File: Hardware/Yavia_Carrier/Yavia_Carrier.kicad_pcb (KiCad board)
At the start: 2 copper layers, 93.5 x 40 mm, 107 parts, among them J1 Power, J10 52610-1572, J11 USB, J12 Ethernet, J2 Serial, J3 STRB_IS, J4 STRB_IS, J5 STRB, J6 STRB, J7 52610-1572, J8 FLASH, J9 FLASH, Q1 MMBT2222ALT1G, Q2 MMBT2222ALT1G, T1 HX1188NL, U1 Verdin iMX8M Plus, U10 LAN9512i, U2 AP63203, U3 LM3671, U4 TCMT1103, U5 TCMT1103, U6 LDD600L, U7 LDD600L, U8 74AHC1G32, U9 74AHC1G32, Y1 25MHZ

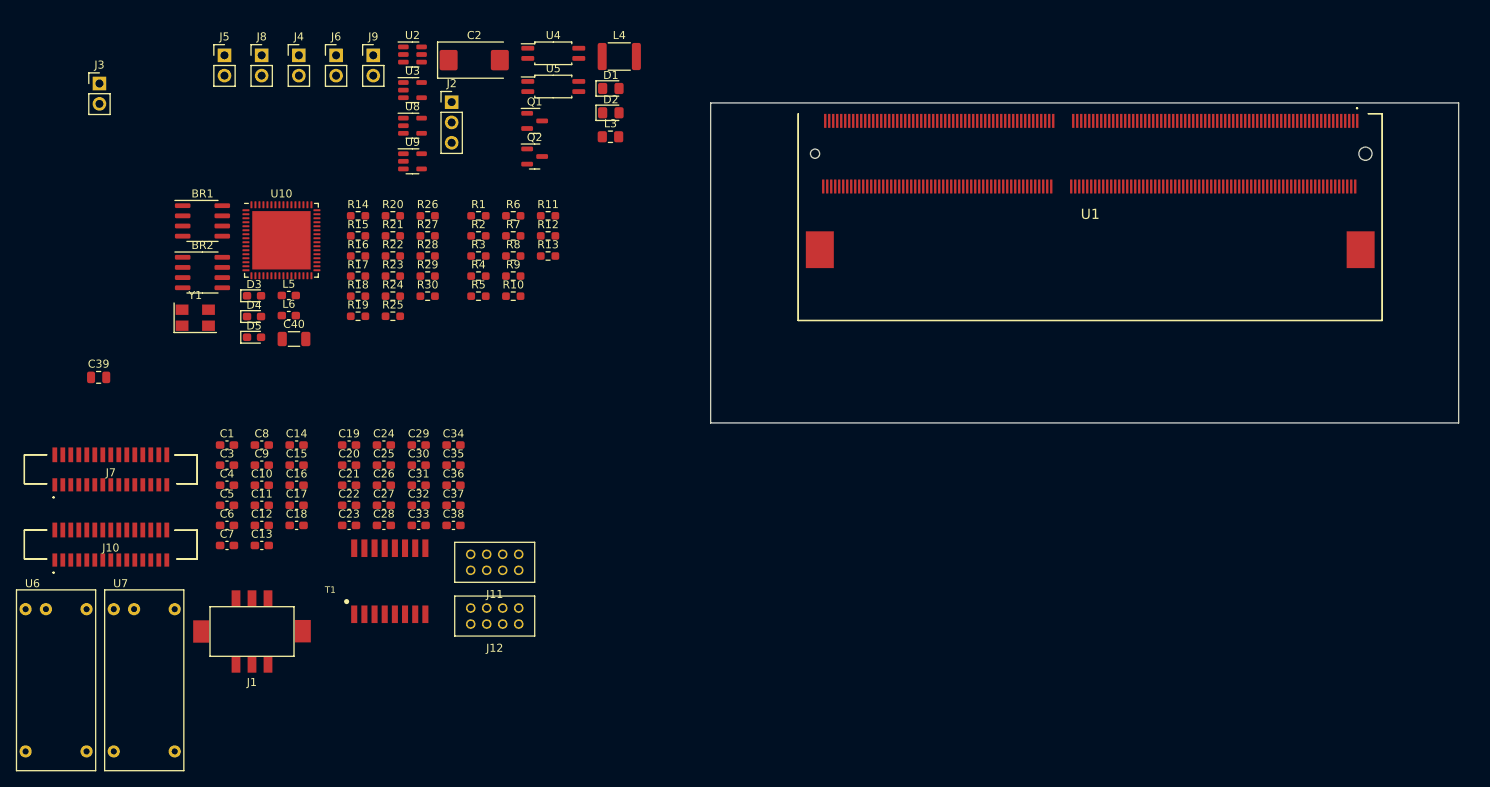
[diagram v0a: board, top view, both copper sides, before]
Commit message: start of component arrangement & add 3d models
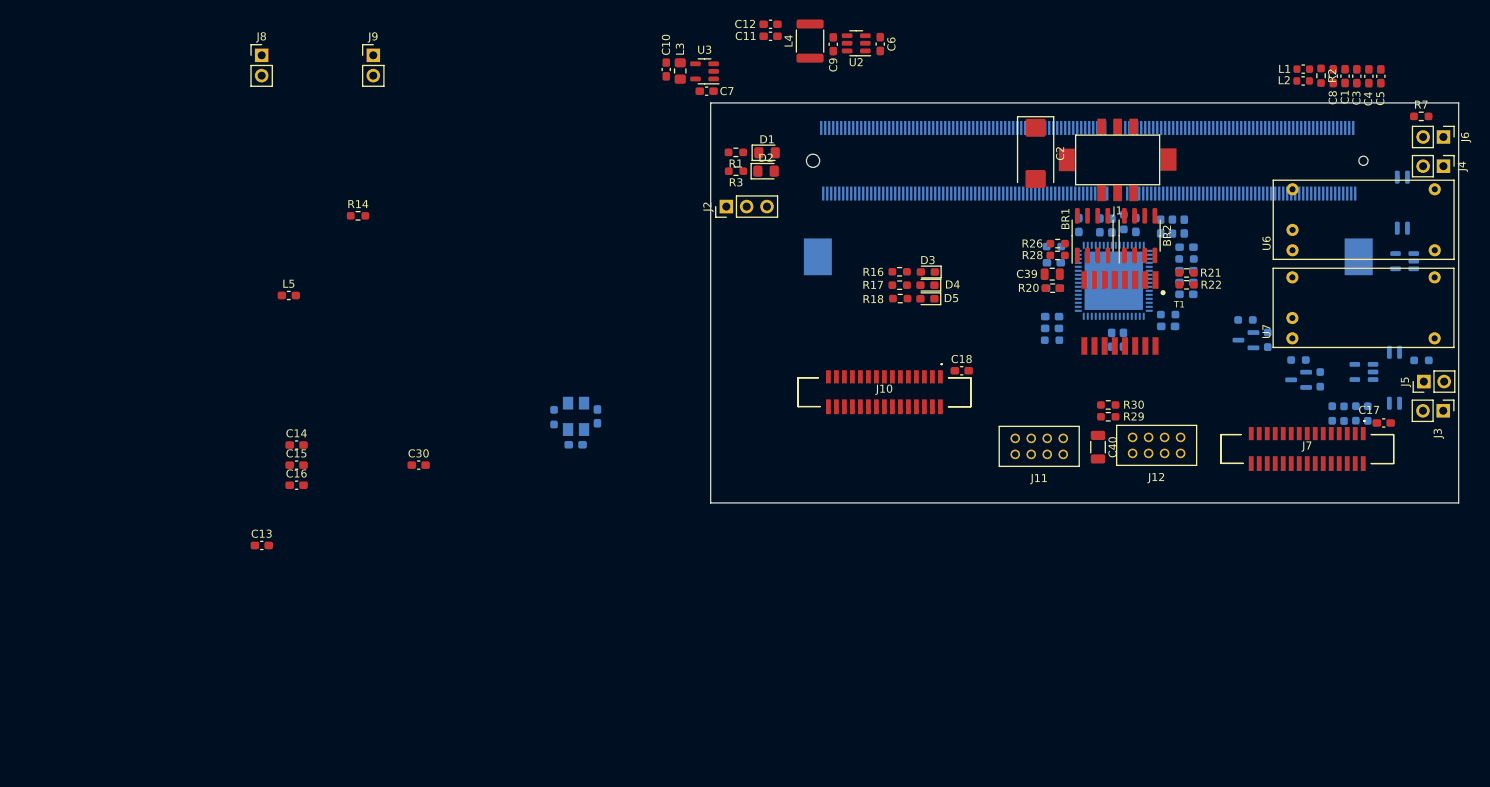
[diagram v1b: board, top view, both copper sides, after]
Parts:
- added L1: 330 ohm/1.7A, Inductor_SMD:L_0603_1608Metric, F.Cu at (224.7, 74.2)
- added L2: 330 ohm/1.7A, Inductor_SMD:L_0603_1608Metric, F.Cu at (224.7, 75.7)
- C19, C20, C21, C22, C23, C24, C25, C26, C27, C28, C29, C31, C32, C33, C34, C35, C36, C37, C38, L6, Q1, Q2, R10, R11, R12, R13, R15, R19, R23, R24, R25, R27, R4, R5, R6, R8, R9, U1, U10, U4, U5, U8, U9, Y1: moved to B.Cu
- moved U6 173.3 mm to (232.2, 93.1), turned to 90 degrees
- moved J3 172.9 mm to (242.2, 117.0), turned to -90 degrees
- moved U7 159.4 mm to (232.2, 104.1), turned to 90 degrees
- moved J5 155.4 mm to (239.8, 113.3), turned to 90 degrees
- moved C5 153.9 mm to (234.4, 75.1), turned to 90 degrees
- moved C4 151.6 mm to (232.9, 75.1), turned to 90 degrees
- moved J7 149.6 mm to (225.2, 121.7), turned to 180 degrees
- moved C3 149.4 mm to (231.4, 75.1), turned to 90 degrees
- moved C1 147.2 mm to (229.9, 75.1), turned to 90 degrees
- moved J4 143.7 mm to (242.2, 86.4), turned to -90 degrees
- moved C8 141.6 mm to (228.4, 75.1), turned to 90 degrees
- moved J6 138.8 mm to (242.2, 82.7), turned to -90 degrees
- moved C17 136.3 mm to (234.7, 118.5)
- moved U9 124.6 mm to (237.3, 98.2), turned to 180 degrees
- moved J1 123.2 mm to (201.5, 85.6)
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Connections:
- J10 pad 10: unconnected-(J10-Pad10) -> /CAM0_IO0
- J10 pad 12: unconnected-(J10-Pad12) -> GND
- J10 pad 14: unconnected-(J10-Pad14) -> /CAM0_CLK+
- J10 pad 16: unconnected-(J10-Pad16) -> /CAM0_CLK-
- J10 pad 18: unconnected-(J10-Pad18) -> GND
- J10 pad 2: unconnected-(J10-Pad2) -> +3V3
- J10 pad 20: unconnected-(J10-Pad20) -> /CAM0_D1+
- J10 pad 22: unconnected-(J10-Pad22) -> /CAM0_D1-
- J10 pad 24: unconnected-(J10-Pad24) -> GND
- J10 pad 26: unconnected-(J10-Pad26) -> /CAM0_D0+
- J10 pad 28: unconnected-(J10-Pad28) -> /CAM0_D0-
- J10 pad 30: unconnected-(J10-Pad30) -> GND
- J10 pad 4: unconnected-(J10-Pad4) -> /CAM0_SDA
- J10 pad 6: unconnected-(J10-Pad6) -> /CAM0_SCL
- J10 pad 8: unconnected-(J10-Pad8) -> /CAM0_IO1
- U1 pad 161: (no net) -> unconnected-(U1F-USB_1_ID-Pad161)
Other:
- board size 93.5 x 40 mm -> 93.5 x 50 mm
